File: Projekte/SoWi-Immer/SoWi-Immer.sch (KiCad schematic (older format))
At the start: 14 parts, among them P1 CONN_01X02, U1 SPV1040

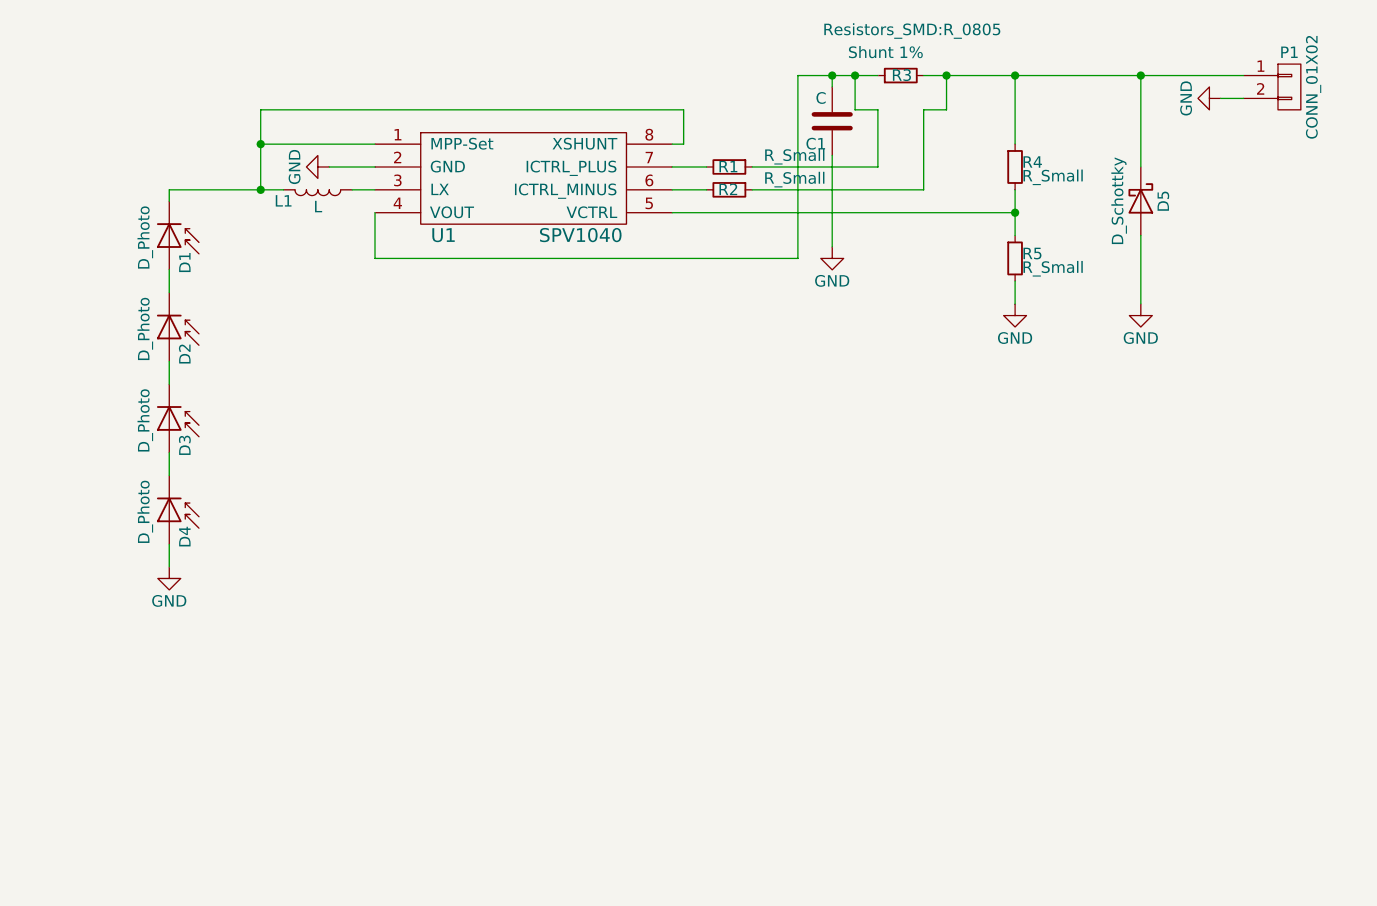
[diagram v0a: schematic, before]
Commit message: Schematic & PCB geändert
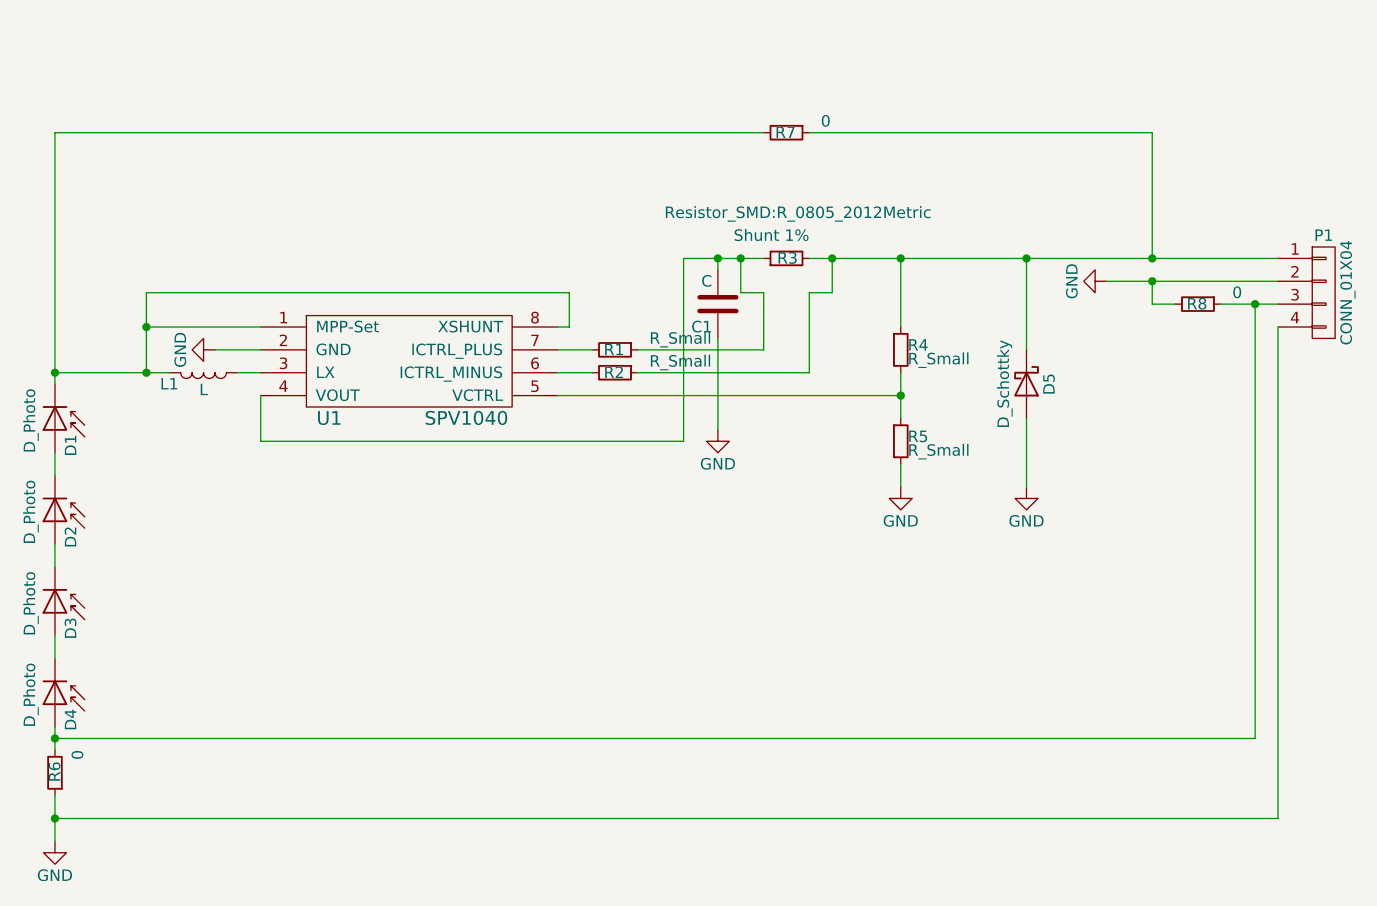
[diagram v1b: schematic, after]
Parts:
- removed P1: CONN_01X02, Resistors_SMD:R_0805, symbol CONN_01X02
- added P1: CONN_01X04, Connector_PinHeader_1.27mm:PinHeader_1x04_P1.27mm_Vertical, symbol CONN_01X04
- added R6, R7, R8: 0, Resistor_SMD:R_0805_2012Metric, symbol R_Small
- C1: footprint Capacitors_SMD:C_1206 -> Capacitor_SMD:C_1206_3216Metric
- L1: footprint Resistors_SMD:R_0805_HandSoldering -> Resistor_SMD:R_0815_2038Metric
- R1, R2, R3, R4, R5: footprint Resistors_SMD:R_0805 -> Resistor_SMD:R_0805_2012Metric
- U1: footprint SSOP_Packages:TSSOP-8_4.4x3mm_Pitch0.65mm -> Package_SSOP:TSSOP-8_4.4x3mm_P0.65mm
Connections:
- net GND: now also P1.2 (P2), P1.4 (P4), R6.1, R8.2; no longer D4.2 (A)
- net at D1.1 (K), L1.2, U1.1 (MPP-Set)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: now also R7.2
- net at D5.1 (K), R2.1, R3.2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: now also P1.1 (P1), R7.1
- new net: D4.2 (A), P1.3 (P3), R6.2, R8.1
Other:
- moved on the sheet: C1, D1, D2, D3, D4, D5, L1, R1, R2, R3, R4, R5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
